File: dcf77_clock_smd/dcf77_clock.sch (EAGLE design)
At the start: 42 parts, among them IC1 7805DT, IC2 ATMEGA48/88/168-AU, J2 DCJ0202, Q2 IRLML6244TRPBF, SW1 EC12E_SW, U1 LCD-16X2SILK, U2 DS1307SO8

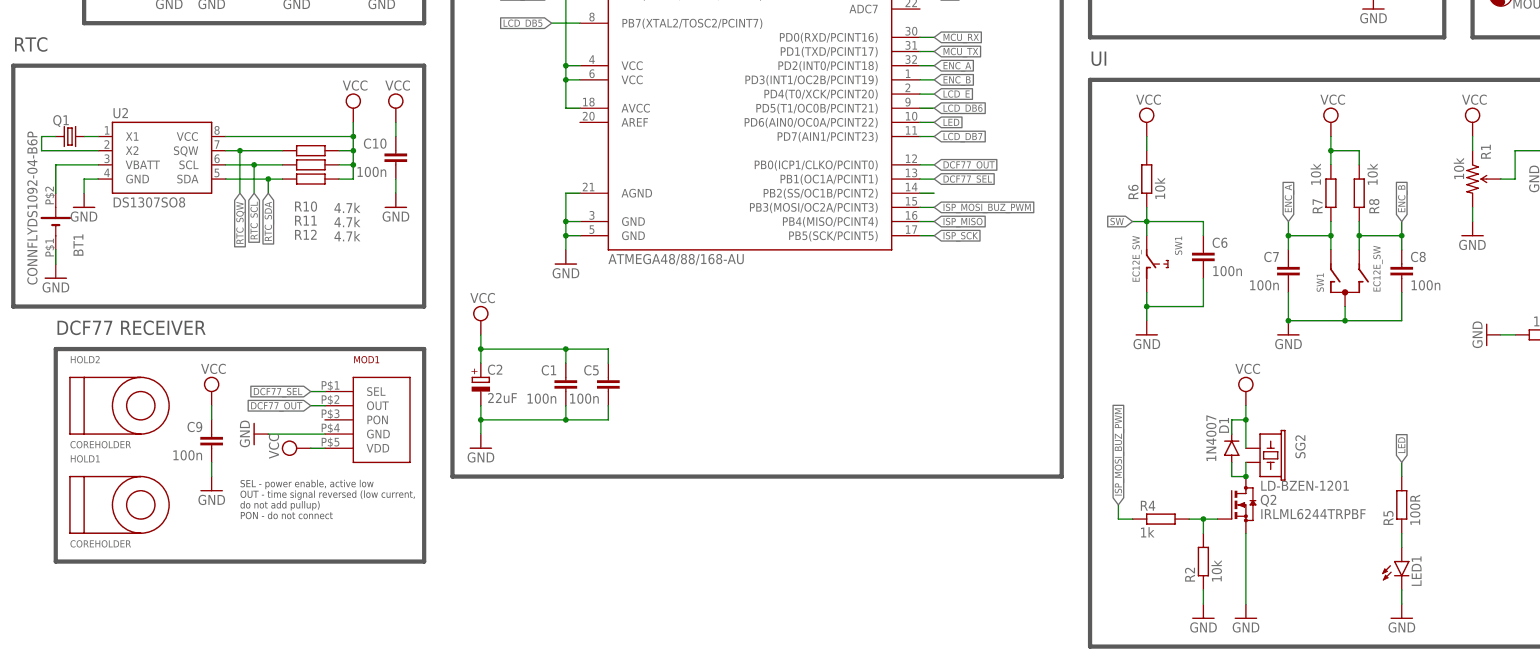
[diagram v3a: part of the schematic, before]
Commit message: ERC fixes
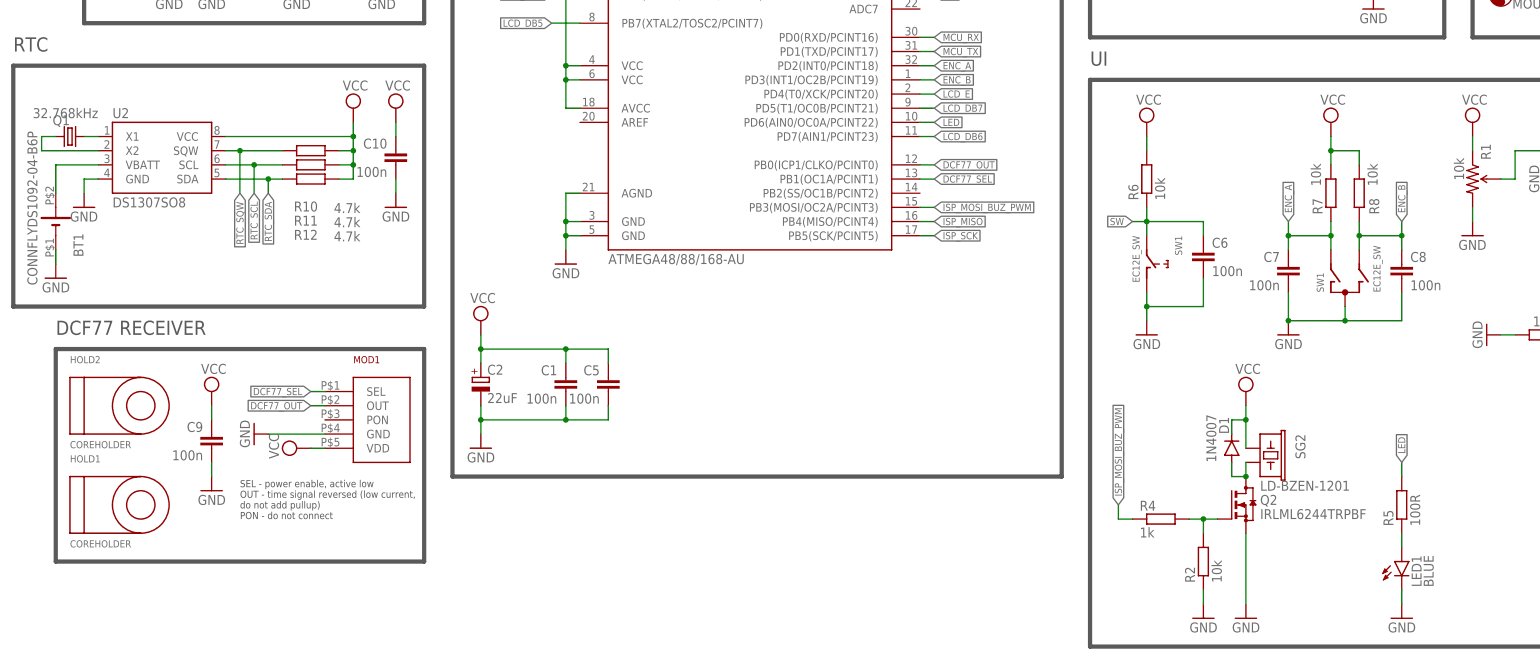
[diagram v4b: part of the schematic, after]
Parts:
- LED1: value (none) -> BLUE
- Q1: value (none) -> 32.768kHz
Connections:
- removed net N$8: IC2.PB2(SS/OC1B/PCINT2)
- net LCD_DB6: now also IC2.PD7(AIN1/PCINT23); no longer IC2.PD5(T1/OC0B/PCINT21)
- net LCD_DB7: now also IC2.PD5(T1/OC0B/PCINT21); no longer IC2.PD7(AIN1/PCINT23)
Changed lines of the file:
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@@
 <part name="U$1" library="SparkFun" deviceset="AVR_SPI_PROG2" device="PTH2"/>
 <part name="U1" library="SparkFun" deviceset="LCD-16X2" device="SILK"/>
-<part name="LED1" library="led" library_urn="urn:adsk.eagle:library:259" deviceset="LED" device="CHIP-LED0805" package3d_urn="urn:adsk.eagle:package:15818/2"/>
+<part name="LED1" library="led" library_urn="urn:adsk.eagle:library:259" deviceset="LED" device="CHIP-LED0805" package3d_urn="urn:adsk.eagle:package:15818/2" value="BLUE"/>
 <part name="IC2" library="atmega8" deviceset="ATMEGA48/88/168" device="-AU"/>
 <part name="U2" library="SparkFun" deviceset="DS1307" device="SO8"/>
 <part name="IC1" library="linear" library_urn="urn:adsk.eagle:library:262" deviceset="78*" device="DT" package3d_urn="urn:adsk.eagle:package:16415/2" technology="05" value="7805DT"/>
 <part name="J2" library="con-jack" library_urn="urn:adsk.eagle:library:154" deviceset="DCJ0202" device="" package3d_urn="urn:adsk.eagle:package:7491/1"/>
-<part name="Q1" library="crystal" library_urn="urn:adsk.eagle:library:204" deviceset="CRYSTAL" device="MM39SL" package3d_urn="urn:adsk.eagle:package:12090/1"/>
+<part name="Q1" library="crystal" library_urn="urn:adsk.eagle:library:204" deviceset="CRYSTAL" device="MM39SL" package3d_urn="urn:adsk.eagle:package:12090/1" value="32.768kHz"/>
 <part name="R1" library="SparkFun" deviceset="TRIMPOT" device="PTH" value="10k"/>
 <part name="H1" library="holes" library_urn="urn:adsk.eagle:library:237" deviceset="MOUNT-HOLE" device="3.2" package3d_urn="urn:adsk.eagle:package:14275/1" value="MOUNT-HOLE3.2"/>
@@
 </segment>
 </net>
-<net name="N$8" class="0">
-<segment>
-<pinref part="IC2" gate="1" pin="PB2(SS/OC1B/PCINT2)"/>
-<wire x1="20.32" y1="40.64" x2="22.86" y2="40.64" width="0.1524" layer="91"/>
-</segment>
-</net>
 <net name="ISP_MISO" class="0">
 <segment>
@@
 </segment>
 <segment>
+<pinref part="IC2" gate="1" pin="PD7(AIN1/PCINT23)"/>
+<wire x1="20.32" y1="50.8" x2="22.86" y2="50.8" width="0.1524" layer="91"/>
+<label x="22.86" y="50.8" size="1.27" layer="95" xref="yes"/>
+</segment>
+</net>
+<net name="LCD_DB7" class="0">
+<segment>
+<pinref part="U1" gate="G$1" pin="DB7"/>
+<wire x1="147.32" y1="20.32" x2="144.78" y2="20.32" width="0.1524" layer="91"/>
+<wire x1="144.78" y1="20.32" x2="142.24" y2="22.86" width="0.1524" layer="91"/>
+</segment>
+<segment>
 <pinref part="IC2" gate="1" pin="PD5(T1/OC0B/PCINT21)"/>
 <wire x1="20.32" y1="55.88" x2="22.86" y2="55.88" width="0.1524" layer="91"/>
 <label x="22.86" y="55.88" size="1.27" layer="95" xref="yes"/>
-</segment>
-</net>
-<net name="LCD_DB7" class="0">
-<segment>
-<pinref part="U1" gate="G$1" pin="DB7"/>
-<wire x1="147.32" y1="20.32" x2="144.78" y2="20.32" width="0.1524" layer="91"/>
-<wire x1="144.78" y1="20.32" x2="142.24" y2="22.86" width="0.1524" layer="91"/>
-</segment>
-<segment>
-<pinref part="IC2" gate="1" pin="PD7(AIN1/PCINT23)"/>
-<wire x1="20.32" y1="50.8" x2="22.86" y2="50.8" width="0.1524" layer="91"/>
-<label x="22.86" y="50.8" size="1.27" layer="95" xref="yes"/>
 </segment>
 </net>
@@
 </sheet>
 </sheets>
+<errors>
+</errors>
 </schematic>
 </drawing>

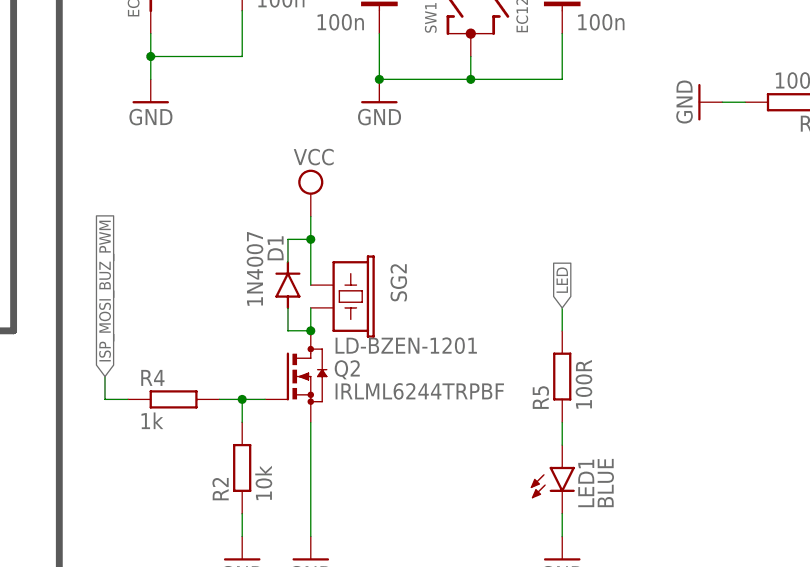
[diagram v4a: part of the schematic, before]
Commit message: Change buzzer footprint
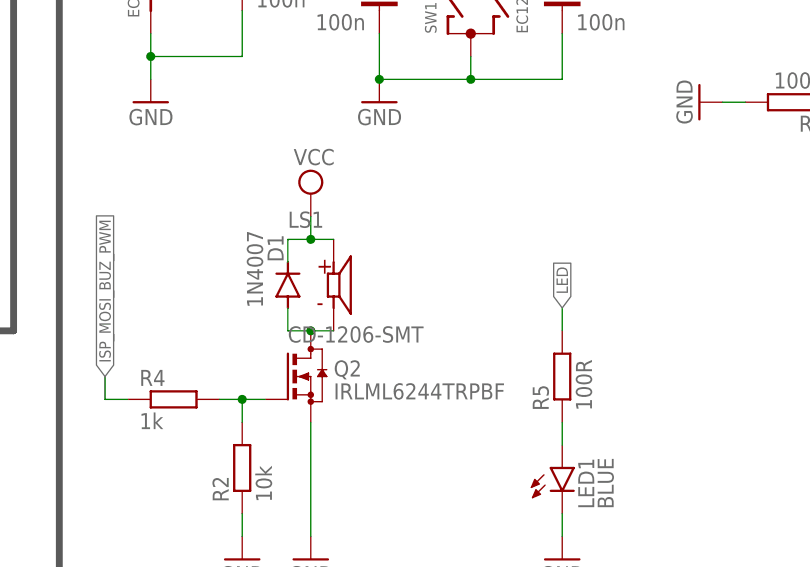
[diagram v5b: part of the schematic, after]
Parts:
- removed SG2: LD-BZEN-1201, SparkFun:BUZZERSMD2-KIT
- added LS1: CD-1206-SMT, CD-1206-SMT:CD-1206-SMT
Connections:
- net N$2: now also LS1.M; no longer SG2.2
- net VCC: now also LS1.P; no longer SG2.1
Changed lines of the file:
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@@
 <part name="H1" library="holes" library_urn="urn:adsk.eagle:library:237" deviceset="MOUNT-HOLE" device="3.2" package3d_urn="urn:adsk.eagle:package:14275/1" value="MOUNT-HOLE3.2"/>
 <part name="D1" library="diode" library_urn="urn:adsk.eagle:library:210" deviceset="DIODE-" device="SOD123" package3d_urn="urn:adsk.eagle:package:43420/1" value="1N4007"/>
-<part name="SG2" library="SparkFun" deviceset="BUZZER" device="SMD2-KIT" value="LD-BZEN-1201"/>
 <part name="BT1" library="_mlokc" deviceset="CONNFLYDS1092-04-B6P" device=""/>
 <part name="R3" library="rcl" library_urn="urn:adsk.eagle:library:334" deviceset="R-EU_" device="M0805" package3d_urn="urn:adsk.eagle:package:23556/2" value="10k"/>
@@
 <part name="SUPPLY15" library="supply2" library_urn="urn:adsk.eagle:library:372" deviceset="VCC" device=""/>
 <part name="GND21" library="supply1" library_urn="urn:adsk.eagle:library:371" deviceset="GND" device=""/>
+<part name="LS1" library="CD-1206-SMT" deviceset="CD-1206-SMT" device=""/>
 </parts>
 <sheets>
@@
 <attribute name="VALUE" x="73.4314" y="-7.62" size="1.778" layer="96" rot="R90"/>
 </instance>
-<instance part="SG2" gate="G$1" x="81.28" y="-5.08" smashed="yes" rot="R270">
-<attribute name="NAME" x="87.63" y="-2.54" size="1.778" layer="95" rot="R270"/>
-<attribute name="VALUE" x="81.28" y="-12.7" size="1.778" layer="96"/>
-</instance>
 <instance part="BT1" gate="G$1" x="-134.62" y="35.56" smashed="yes" rot="MR90">
 <attribute name="NAME" x="-131.445" y="29.21" size="1.778" layer="95" rot="MR90"/>
@@
 <instance part="GND21" gate="1" x="-73.66" y="38.1" smashed="yes" rot="MR0">
 <attribute name="VALUE" x="-71.12" y="35.56" size="1.778" layer="96" rot="MR0"/>
+</instance>
+<instance part="LS1" gate="G$1" x="81.28" y="-5.08" smashed="yes">
+<attribute name="NAME" x="76.18125" y="1.29345" size="1.784559375" layer="95"/>
+<attribute name="VALUE" x="76.17583125" y="-11.46021875" size="1.78646875" layer="96"/>
 </instance>
 </instances>
@@
 <pinref part="SUPPLY7" gate="G$1" pin="VCC"/>
 <wire x1="78.74" y1="0" x2="78.74" y2="2.54" width="0.1524" layer="91"/>
+<pinref part="LS1" gate="G$1" pin="P"/>
+<wire x1="78.74" y1="0" x2="81.28" y2="0" width="0.1524" layer="91"/>
 <junction x="78.74" y="0"/>
-<pinref part="SG2" gate="G$1" pin="1"/>
-<wire x1="78.74" y1="0" x2="78.74" y2="-5.08" width="0.1524" layer="91"/>
 </segment>
 <segment>
@@
 <pinref part="D1" gate="G$1" pin="A"/>
 <wire x1="76.2" y1="-10.16" x2="76.2" y2="-7.62" width="0.1524" layer="91"/>
-<pinref part="SG2" gate="G$1" pin="2"/>
-<wire x1="78.74" y1="-7.62" x2="78.74" y2="-10.16" width="0.1524" layer="91"/>
+<pinref part="LS1" gate="G$1" pin="M"/>
+<wire x1="78.74" y1="-10.16" x2="81.28" y2="-10.16" width="0.1524" layer="91"/>
 <junction x="78.74" y="-10.16"/>
 </segment>

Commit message: Allign mounting holes
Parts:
- HOLD1, HOLD2: value COREHOLDER -> COREHOLDERH6P; device dcf77:COREHOLDER -> dcf77:COREHOLDERH6P
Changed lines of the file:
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@@
 <grid distance="0.1" unitdist="inch" unit="inch" style="lines" multiple="1" display="yes" altdistance="0.01" altunitdist="inch" altunit="inch"/>
 <layers>
-<layer number="1" name="Top" color="4" fill="1" visible="no" active="no"/>
-<layer number="16" name="Bottom" color="1" fill="1" visible="no" active="no"/>
-<layer number="17" name="Pads" color="2" fill="1" visible="no" active="no"/>
-<layer number="18" name="Vias" color="2" fill="1" visible="no" active="no"/>
-<layer number="19" name="Unrouted" color="6" fill="1" visible="no" active="no"/>
-<layer number="20" name="Dimension" color="24" fill="1" visible="no" active="no"/>
-<layer number="21" name="tPlace" color="7" fill="1" visible="no" active="no"/>
-<layer number="22" name="bPlace" color="7" fill="1" visible="no" active="no"/>
-<layer number="23" name="tOrigins" color="15" fill="1" visible="no" active="no"/>
-<layer number="24" name="bOrigins" color="15" fill="1" visible="no" active="no"/>
-<layer number="25" name="tNames" color="7" fill="1" visible="no" active="no"/>
-<layer number="26" name="bNames" color="7" fill="1" visible="no" active="no"/>
-<layer number="27" name="tValues" color="7" fill="1" visible="no" active="no"/>
-<layer number="28" name="bValues" color="7" fill="1" visible="no" active="no"/>
+<layer number="1" name="Top" color="4" fill="1" visible="yes" active="no"/>
+<layer number="16" name="Bottom" color="1" fill="1" visible="yes" active="no"/>
+<layer number="17" name="Pads" color="2" fill="1" visible="yes" active="no"/>
+<layer number="18" name="Vias" color="2" fill="1" visible="yes" active="no"/>
+<layer number="19" name="Unrouted" color="6" fill="1" visible="yes" active="no"/>
+<layer number="20" name="Dimension" color="24" fill="1" visible="yes" active="no"/>
+<layer number="21" name="tPlace" color="7" fill="1" visible="yes" active="no"/>
+<layer number="22" name="bPlace" color="7" fill="1" visible="yes" active="no"/>
+<layer number="23" name="tOrigins" color="15" fill="1" visible="yes" active="no"/>
+<layer number="24" name="bOrigins" color="15" fill="1" visible="yes" active="no"/>
+<layer number="25" name="tNames" color="7" fill="1" visible="yes" active="no"/>
+<layer number="26" name="bNames" color="7" fill="1" visible="yes" active="no"/>
+<layer number="27" name="tValues" color="7" fill="1" visible="yes" active="no"/>
+<layer number="28" name="bValues" color="7" fill="1" visible="yes" active="no"/>
 <layer number="29" name="tStop" color="7" fill="3" visible="no" active="no"/>
 <layer number="30" name="bStop" color="7" fill="6" visible="no" active="no"/>
@@
 <layer number="35" name="tGlue" color="7" fill="4" visible="no" active="no"/>
 <layer number="36" name="bGlue" color="7" fill="5" visible="no" active="no"/>
-<layer number="37" name="tTest" color="7" fill="1" visible="no" active="no"/>
-<layer number="38" name="bTest" color="7" fill="1" visible="no" active="no"/>
+<layer number="37" name="tTest" color="7" fill="1" visible="yes" active="no"/>
+<layer number="38" name="bTest" color="7" fill="1" visible="yes" active="no"/>
 <layer number="39" name="tKeepout" color="4" fill="11" visible="no" active="no"/>
 <layer number="40" name="bKeepout" color="1" fill="11" visible="no" active="no"/>
@@
 <layer number="44" name="Drills" color="7" fill="1" visible="no" active="no"/>
 <layer number="45" name="Holes" color="7" fill="1" visible="no" active="no"/>
-<layer number="46" name="Milling" color="3" fill="1" visible="no" active="no"/>
-<layer number="47" name="Measures" color="7" fill="1" visible="no" active="no"/>
-<layer number="48" name="Document" color="7" fill="1" visible="no" active="no"/>
-<layer number="49" name="Reference" color="7" fill="1" visible="no" active="no"/>
-<layer number="50" name="dxf" color="7" fill="1" visible="no" active="no"/>
-<layer number="51" name="tDocu" color="7" fill="1" visible="no" active="no"/>
-<layer number="52" name="bDocu" color="7" fill="1" visible="no" active="no"/>
-<layer number="53" name="tGND_GNDA" color="7" fill="9" visible="no" active="no"/>
-<layer number="54" name="bGND_GNDA" color="1" fill="9" visible="no" active="no"/>
-<layer number="56" name="wert" color="7" fill="1" visible="no" active="no"/>
+<layer number="46" name="Milling" color="3" fill="1" visible="yes" active="no"/>
+<layer number="47" name="Measures" color="7" fill="1" visible="yes" active="no"/>
+<layer number="48" name="Document" color="7" fill="1" visible="yes" active="no"/>
+<layer number="49" name="Reference" color="7" fill="1" visible="yes" active="no"/>
+<layer number="50" name="dxf" color="7" fill="1" visible="yes" active="no"/>
+<layer number="51" name="tDocu" color="7" fill="1" visible="yes" active="no"/>
+<layer number="52" name="bDocu" color="7" fill="1" visible="yes" active="no"/>
+<layer number="53" name="tGND_GNDA" color="7" fill="9" visible="yes" active="no"/>
+<layer number="54" name="bGND_GNDA" color="1" fill="9" visible="yes" active="no"/>
+<layer number="56" name="wert" color="7" fill="1" visible="yes" active="no"/>
 <layer number="88" name="SimResults" color="9" fill="1" visible="yes" active="yes"/>
 <layer number="89" name="SimProbes" color="9" fill="1" visible="yes" active="yes"/>
@@
 <part name="C2" library="rcl" library_urn="urn:adsk.eagle:library:334" deviceset="CPOL-EU" device="UD-4X5,8" package3d_urn="urn:adsk.eagle:package:23474/1" value="22uF"/>
 <part name="MOD1" library="dcf77" deviceset="DCF77MODULE" device=""/>
-<part name="HOLD1" library="dcf77" deviceset="COREHOLDER" device=""/>
-<part name="HOLD2" library="dcf77" deviceset="COREHOLDER" device=""/>
+<part name="HOLD1" library="dcf77" deviceset="COREHOLDER" device="H6P"/>
+<part name="HOLD2" library="dcf77" deviceset="COREHOLDER" device="H6P"/>
 <part name="H2" library="holes" library_urn="urn:adsk.eagle:library:237" deviceset="MOUNT-HOLE" device="3.2" package3d_urn="urn:adsk.eagle:package:14275/1" value="MOUNT-HOLE3.2"/>
 <part name="H3" library="holes" library_urn="urn:adsk.eagle:library:237" deviceset="MOUNT-HOLE" device="3.2" package3d_urn="urn:adsk.eagle:package:14275/1" value="MOUNT-HOLE3.2"/>
